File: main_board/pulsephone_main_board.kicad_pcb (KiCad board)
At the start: 4 copper layers, 70.5 x 128.5 mm, 51 parts, among them J1 USB_C_Receptacle_USB2.0_14P, J2 Conn_01x05, J3 Conn_2Rows-35Pins_MountingPin, J4 Conn_2Rows-35Pins_MountingPin, J5 Conn_2Rows-35Pins_MountingPin, J7 Micro_SD_Card_Det1, SW1 SW_Push, SW2 SW_Push, U1 XL1509-3.3, U2 PCM5102APWR, U5 TP4056-42-ESOP8

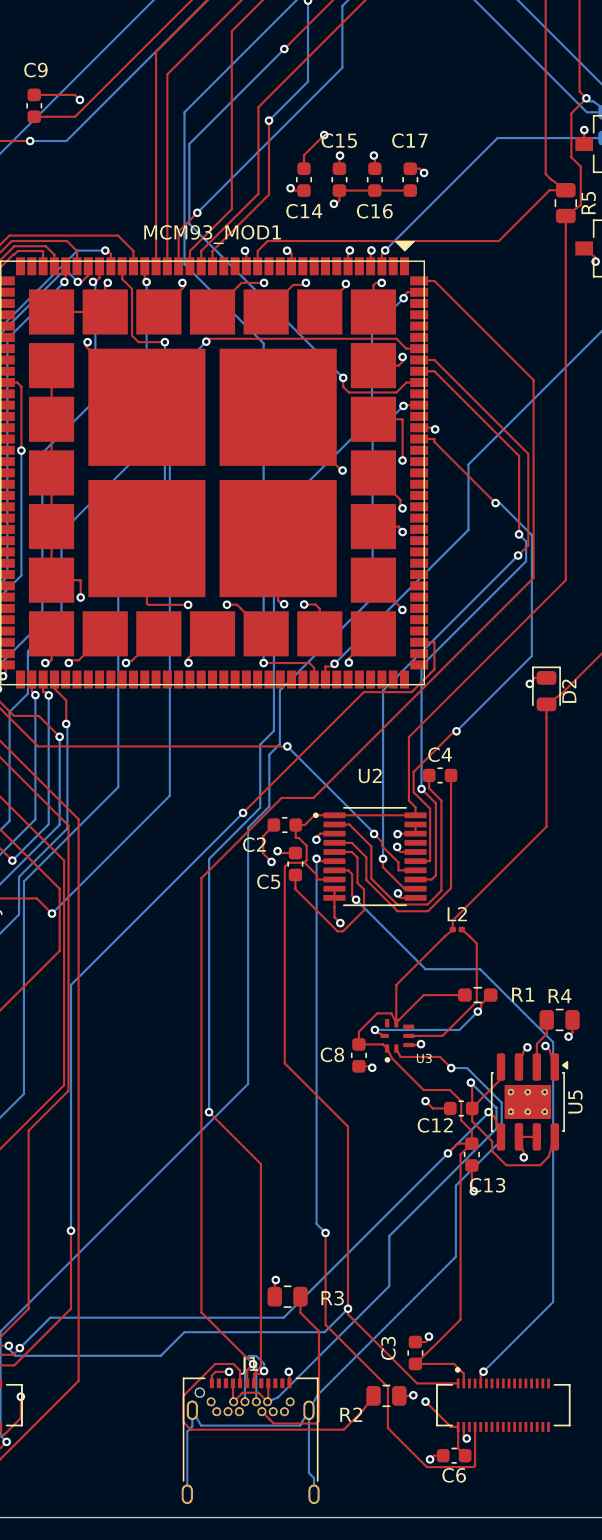
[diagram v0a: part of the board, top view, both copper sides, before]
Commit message: more smoothing caps, and making sure board is compliant with CompuLab Standards
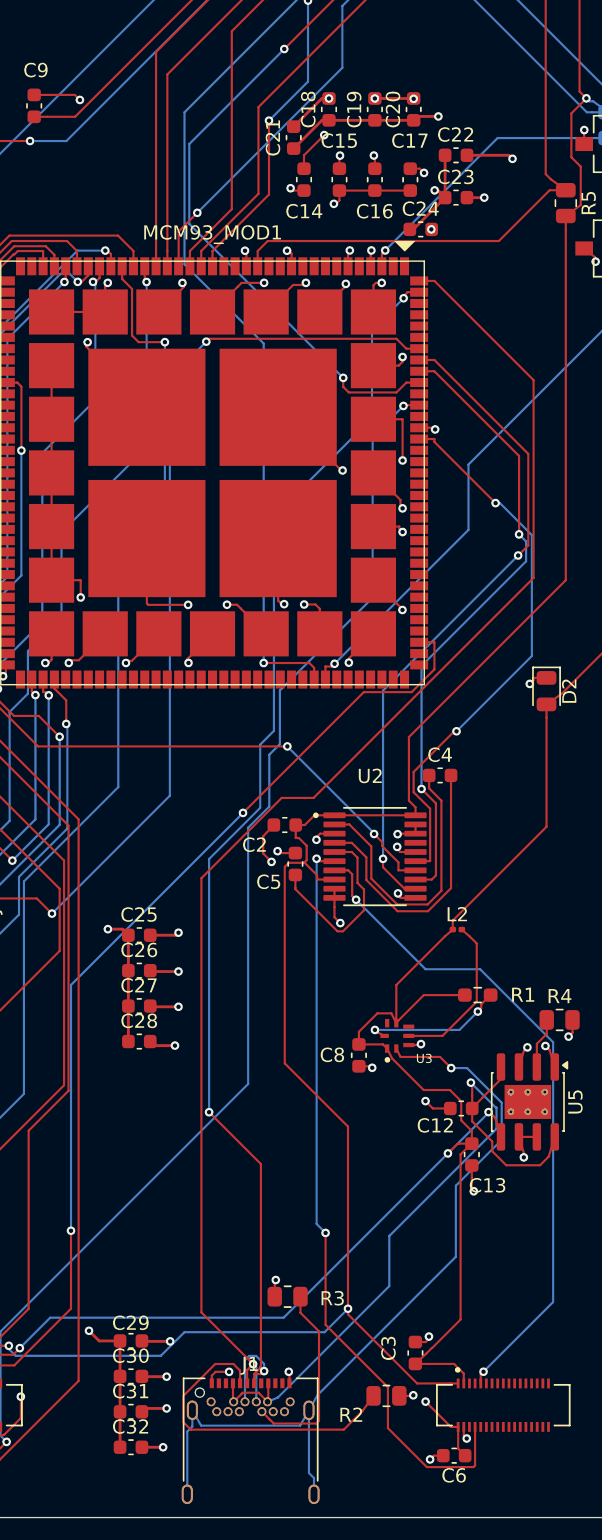
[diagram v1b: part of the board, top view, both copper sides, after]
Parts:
- added C18: 22uF, Capacitor_SMD:C_0603_1608Metric, F.Cu at (143.2, 54.8)
- added C19: 22uF, Capacitor_SMD:C_0603_1608Metric, F.Cu at (146.5, 54.8)
- added C20: 22uF, Capacitor_SMD:C_0603_1608Metric, F.Cu at (149.2, 54.8)
- added C21: 22uF, Capacitor_SMD:C_0603_1608Metric, F.Cu at (140.8, 56.8)
- added C22: 22uF, Capacitor_SMD:C_0603_1608Metric, F.Cu at (152.2, 58.0)
- added C23: 22uF, Capacitor_SMD:C_0603_1608Metric, F.Cu at (152.2, 61.0)
- added C24: 22uF, Capacitor_SMD:C_0603_1608Metric, F.Cu at (149.8, 63.2)
- added C25: 22uF, Capacitor_SMD:C_0603_1608Metric, F.Cu at (129.8, 113.2)
- added C26: 22uF, Capacitor_SMD:C_0603_1608Metric, F.Cu at (129.8, 115.8)
- added C27: 22uF, Capacitor_SMD:C_0603_1608Metric, F.Cu at (129.8, 118.3)
- added C28: 22uF, Capacitor_SMD:C_0603_1608Metric, F.Cu at (129.8, 120.8)
- added C29: 22uF, Capacitor_SMD:C_0603_1608Metric, F.Cu at (129.2, 142.0)
- added C30: 22uF, Capacitor_SMD:C_0603_1608Metric, F.Cu at (129.2, 144.5)
- added C31: 22uF, Capacitor_SMD:C_0603_1608Metric, F.Cu at (129.2, 147.0)
- added C32: 22uF, Capacitor_SMD:C_0603_1608Metric, F.Cu at (129.2, 149.5)
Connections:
- MCM93_MOD1 pad 76: unconnected-(MCM93_MOD1C-6-Pad76) -> SD2_CD_B
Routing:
- net +5V: track 32.2 -> 70.0 mm, vias 12 -> 16
- net GND: track 213.5 -> 239.2 mm, vias 81 -> 95

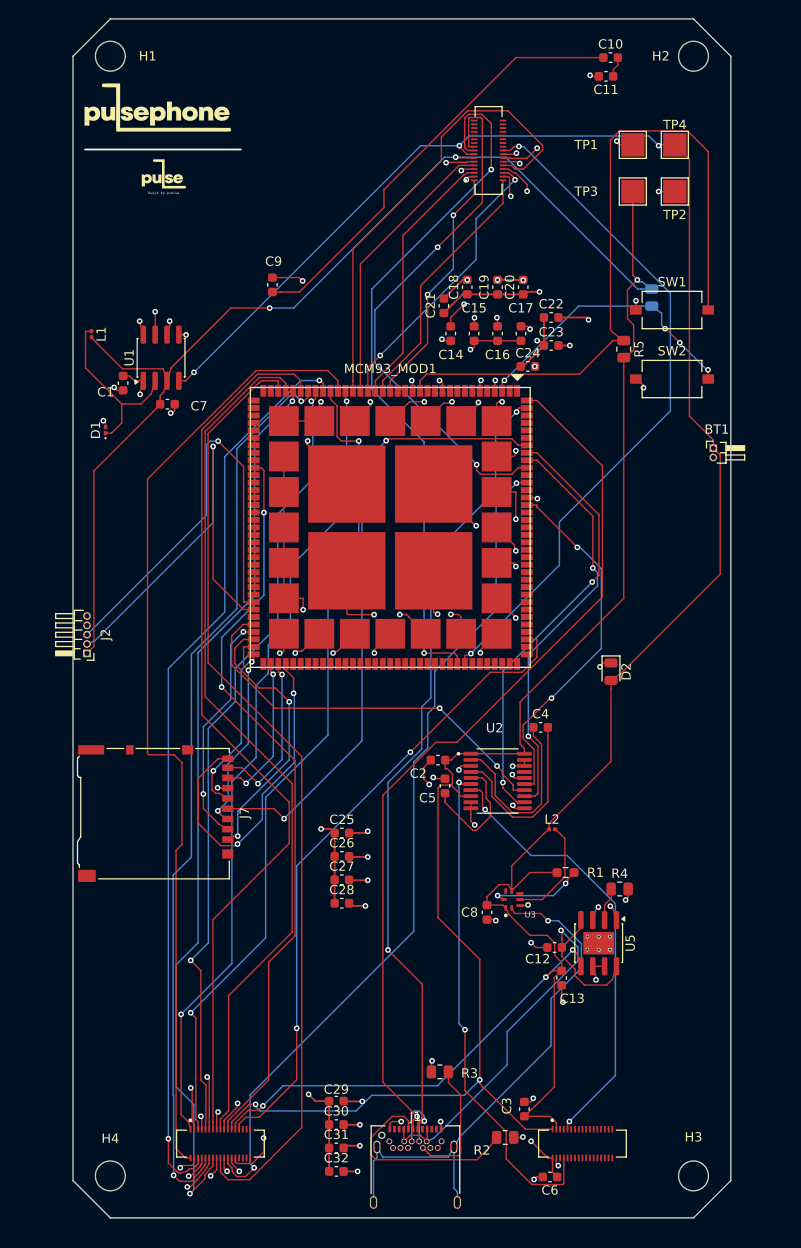
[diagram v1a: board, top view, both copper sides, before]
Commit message: fix PCB design errors, and fix power LED circuitry.
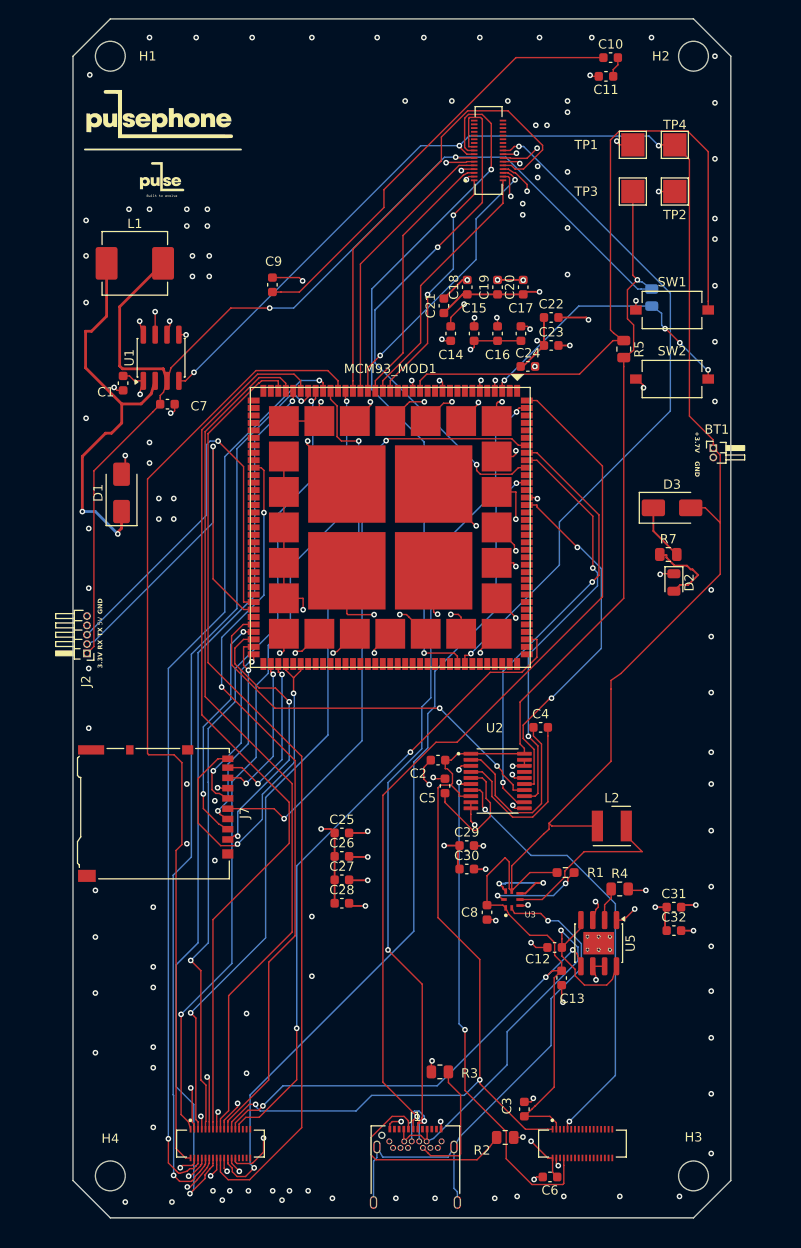
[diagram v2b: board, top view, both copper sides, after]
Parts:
- added D3: D_Schottky, Diode_SMD:D_SMA, F.Cu at (165.2, 78.4)
- added R7: 1kΩ, Resistor_SMD:R_0805_2012Metric, F.Cu at (164.8, 83.4)
- C1, C7: value 20uF -> 22uF
- D1: footprint Diode_SMD:D_0201_0603Metric -> Diode_SMD:D_SMA
- L1: footprint Inductor_SMD:L_0201_0603Metric -> Inductor_SMD:L_APV_APH0650
- L2: footprint Inductor_SMD:L_0201_0603Metric -> Inductor_SMD_Wurth:L_Wurth_WE-LQSH-4020
- moved C32 44.4 mm to (165.4, 123.7)
- moved C31 44.4 mm to (165.4, 121.2)
- moved C29 30.7 mm to (143.2, 114.6)
- moved C30 30.7 mm to (143.2, 117.1)
- moved D2 11.7 mm to (165.4, 86.4)
- moved L1 8.90 mm to (107.6, 52.2), turned to 0 degrees
- moved D1 6.93 mm to (106.2, 76.8)
- moved L2 6.42 mm to (158.8, 112.5)
- moved G*** 0.73 mm to (110.2, 36.2)
- moved G*** 0.36 mm to (110.5, 43.3)
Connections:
- D2 pad 2: +3.7VBAT -> Net-(D2-A)
- U3 pad 5: (no net) -> +5V
- U3 pad 7: (no net) -> +5V
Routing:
- net Net-(D1-K): track 19.3 -> 44.1 mm, vias 0 -> 2
- net +3.7VBAT: track 250.8 -> 265.1 mm
- net +3.3V: track 271.3 -> 279.9 mm
- net Net-(D2-A): track 0.00 -> 8.49 mm
- net Net-(U3-SW): track 11.4 -> 19.1 mm
- net +5V: track 70.0 -> 76.3 mm, vias 16 -> 19
- net Net-(D3-K): track 0.00 -> 6.04 mm
- net GND: track 239.2 -> 241.6 mm, vias 95 -> 200
- net SD2_CD_B: track 36.3 -> 38.1 mm
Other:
- board text added: "+3.7V"
- board text added: "3.3V"
- board text added: "5V"
- board text added: "GND"
- board text added: "RX"
- board text added: "TX"

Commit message: git stuff
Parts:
- L1: footprint Inductor_SMD:L_APV_APH0650 -> Inductor_SMD:L_APV_APH0630
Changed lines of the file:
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@@
 		)
 	)
-	(footprint "Inductor_SMD:L_APV_APH0650"
+	(footprint "Inductor_SMD:L_APV_APH0630"
 		(layer "F.Cu")
 		(at 107.625 52.2)
-		(descr "Inductor, APV, APH0650, 6.8x6.6x4.8mm, (http://en.apvind.com/public/upload/20240408/996aafa961154ed753e4983e7eb80fa7.pdf), generated with kicad-footprint-generator gen_inductor.py")
+		(descr "Inductor, APV, APH0630, 6.8x6.6x2.8mm, (http://en.apvind.com/public/upload/20240408/996aafa961154ed753e4983e7eb80fa7.pdf), generated with kicad-footprint-generator gen_inductor.py")
 		(tags "molded power shielded")
 		(property "Reference" "L1"
@@
 			)
 		)
-		(property "Datasheet" "~"
+		(property "Datasheet" ""
 			(at 0 0 0)
 			(layer "F.Fab")
@@
 			)
 		)
-		(property "Description" "Inductor"
+		(property "Description" ""
 			(at 0 0 0)
 			(layer "F.Fab")
@@
 		)
 		(embedded_fonts no)
-		(model "${KICAD9_3DMODEL_DIR}/Inductor_SMD.3dshapes/L_APV_APH0650.step"
+		(model "${KICAD9_3DMODEL_DIR}/Inductor_SMD.3dshapes/L_APV_APH0630.step"
 			(offset
 				(xyz 0 0 0)

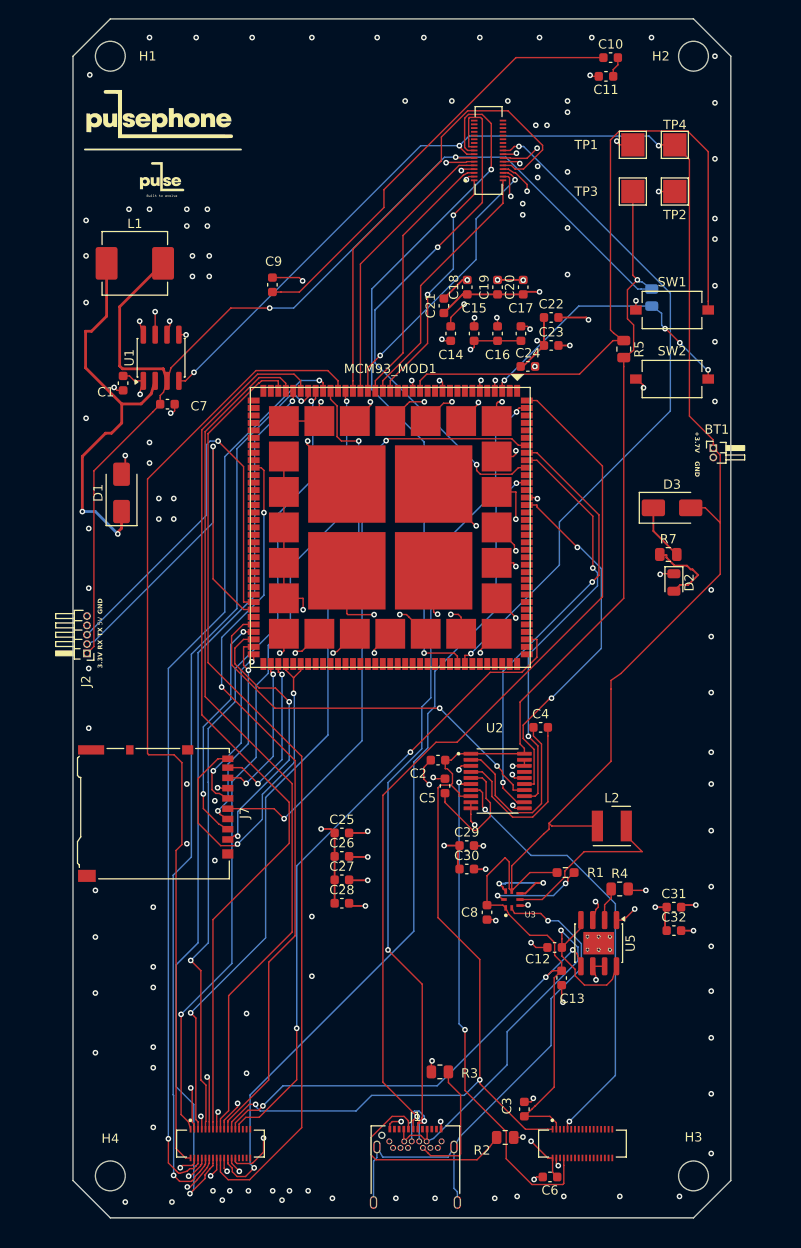
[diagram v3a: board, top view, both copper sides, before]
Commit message: add 3.7v regulator to VBAT for a stable vbat voltage.
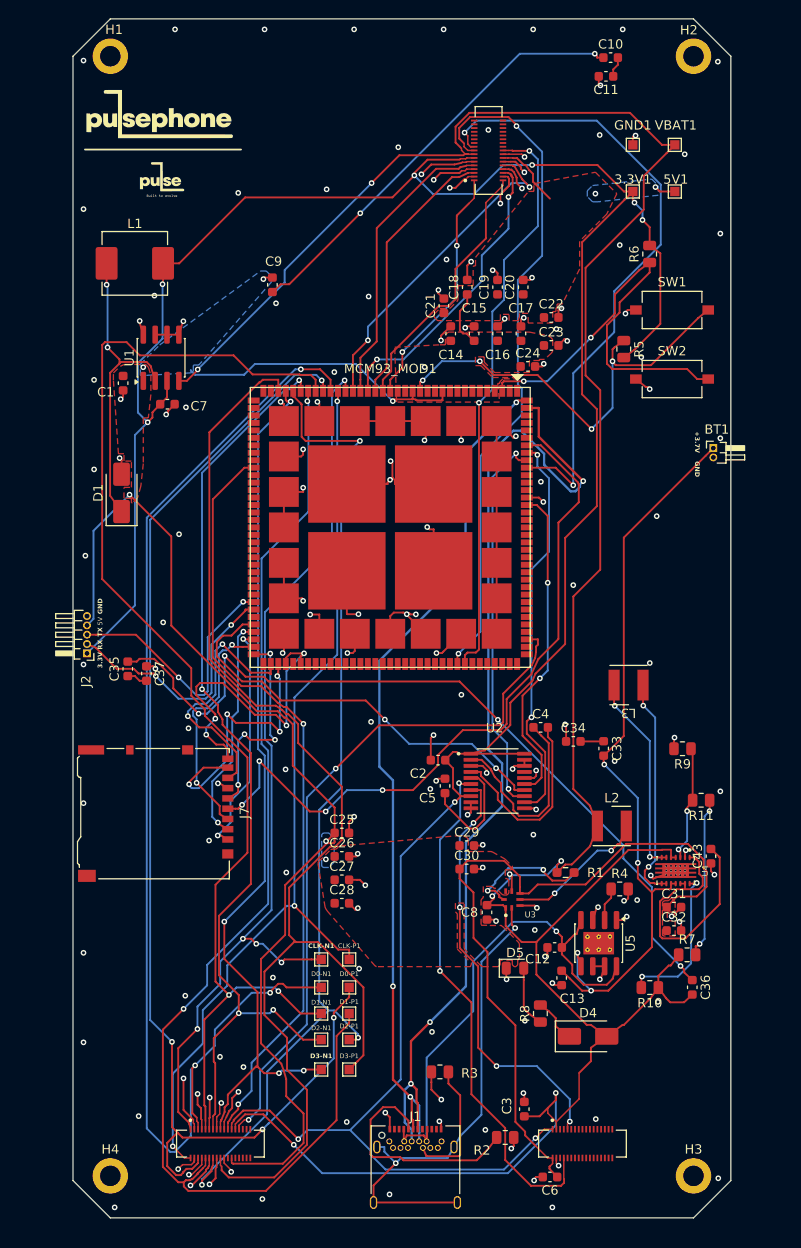
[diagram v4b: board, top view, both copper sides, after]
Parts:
- removed D2: LED, LED_SMD:LED_0805_2012Metric
- removed D3: D_Schottky, Diode_SMD:D_SMA
- added C33: 10uF, Capacitor_SMD:C_0603_1608Metric, F.Cu at (157.9, 104.2)
- added C34: 10uF, Capacitor_SMD:C_0603_1608Metric, F.Cu at (154.6, 103.4)
- added C35: 22uF, Capacitor_SMD:C_0603_1608Metric, F.Cu at (106.9, 95.7)
- added C36: 22uF, Capacitor_SMD:C_0603_1608Metric, F.Cu at (167.4, 129.8)
- added C37: 22uF, Capacitor_SMD:C_0603_1608Metric, F.Cu at (108.9, 96.2)
- added C43: 100nF, Capacitor_SMD:C_0603_1608Metric, F.Cu at (169.4, 115.7)
- added CLK-N1: TestPoint, TestPoint:TestPoint_Pad_1.0x1.0mm, F.Cu at (127.6, 126.8)
- added CLK-P1: TestPoint, TestPoint:TestPoint_Pad_1.0x1.0mm, F.Cu at (130.6, 126.8)
- added D0-N1: TestPoint, TestPoint:TestPoint_Pad_1.0x1.0mm, F.Cu at (127.6, 129.8)
- added D0-P1: TestPoint, TestPoint:TestPoint_Pad_1.0x1.0mm, F.Cu at (130.6, 129.8)
- added D1-N1: TestPoint, TestPoint:TestPoint_Pad_1.0x1.0mm, F.Cu at (127.6, 132.6)
- added D1-P1: TestPoint, TestPoint:TestPoint_Pad_1.0x1.0mm, F.Cu at (130.6, 132.6)
- added D2-N1: TestPoint, TestPoint:TestPoint_Pad_1.0x1.0mm, F.Cu at (127.6, 135.4)
- added D2-P1: TestPoint, TestPoint:TestPoint_Pad_1.0x1.0mm, F.Cu at (130.6, 135.4)
- added D3-N1: TestPoint, TestPoint:TestPoint_Pad_1.0x1.0mm, F.Cu at (127.6, 138.6)
- added D3-P1: TestPoint, TestPoint:TestPoint_Pad_1.0x1.0mm, F.Cu at (130.6, 138.6)
- added D4: D_Schottky, Diode_SMD:D_SMA, F.Cu at (156.2, 135.0)
- added D5: LED, LED_SMD:LED_0805_2012Metric, F.Cu at (148.4, 127.7)
- added L3: 1.5uH, Inductor_SMD_Wurth:L_Wurth_WE-LQSH-4020, F.Cu at (160.5, 97.4)
- added R10: 1 MΩ, Resistor_SMD:R_0805_2012Metric, F.Cu at (162.8, 129.8)
- added R11: 51 kΩ, Resistor_SMD:R_0805_2012Metric, F.Cu at (168.3, 109.7)
- added R8: 1kΩ, Resistor_SMD:R_0805_2012Metric, F.Cu at (151.1, 132.6)
- added R9: 180 kΩ, Resistor_SMD:R_0805_2012Metric, F.Cu at (166.3, 104.2)
- added U4: TPS63020DSJR/3.7V Reg, TPS63020:IC_TPS63020DSJR, F.Cu at (165.6, 117.3)
- 3.3V1: renamed from TP3; footprint TestPoint:TestPoint_Pad_2.5x2.5mm -> TestPoint:TestPoint_Pad_1.0x1.0mm
- 5V1: renamed from TP2; footprint TestPoint:TestPoint_Pad_2.5x2.5mm -> TestPoint:TestPoint_Pad_1.0x1.0mm
- GND1: renamed from TP1; footprint TestPoint:TestPoint_Pad_2.5x2.5mm -> TestPoint:TestPoint_Pad_1.0x1.0mm
- H1, H2, H3, H4: footprint MountingHole:MountingHole_3.2mm_M3 -> MountingHole:MountingHole_2.2mm_M2_DIN965_Pad
- R6: moved to F.Cu
- R7: value 1kΩ -> 1.1 MΩ
- VBAT1: renamed from TP4; footprint TestPoint:TestPoint_Pad_2.5x2.5mm -> TestPoint:TestPoint_Pad_1.0x1.0mm
- moved R7 43.0 mm to (166.8, 126.3)
- moved R6 4.67 mm to (162.8, 51.2)
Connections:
- BT1 pad 1: +3.7VBAT -> Net-(BT1-+)
- C13 pad 2: +3.7VBAT -> Net-(BT1-+)
- R7 pad 1: Net-(D2-A) -> +3.7VBAT
- U5 pad 5: +3.7VBAT -> Net-(BT1-+)
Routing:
- net +5V: track 76.3 -> 238.2 mm, vias 19 -> 8
- net /I2C3_SDA: track 91.1 -> 0.00 mm, vias 2 -> 0
- net Net-(C35-Pad2): track 0.00 -> 87.3 mm, vias 0 -> 4
- net Net-(BT1-+): track 0.00 -> 82.4 mm, vias 0 -> 4
- net /DSI_D1_N: track 85.6 -> 131.0 mm
- net /DSI_D0_N: track 89.3 -> 133.2 mm, vias 2 -> 3
- net /DSI_D0_P: track 97.7 -> 130.8 mm, vias 2 -> 4
- net /DSI_D1_P: track 97.1 -> 129.3 mm
- net /DSI_D3_P: track 102.4 -> 131.9 mm
- net RESET: track 75.7 -> 47.1 mm, vias 0 -> 4
- net +3.7VBAT: track 265.1 -> 293.6 mm, vias 6 -> 7
- net Net-(U4-EN): track 0.00 -> 28.4 mm
- net L_1: track 0.00 -> 24.2 mm, vias 0 -> 2
- net +3.3V: track 279.9 -> 302.8 mm, vias 5 -> 9
- net L_2: track 0.00 -> 21.8 mm, vias 0 -> 2
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- added copper zone on B.Cu, net +5V
- added copper zone on F.Cu, net +5V
- added copper zone on In2.Cu, net GND
- removed copper zone on In2.Cu, net +5V

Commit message: fixes
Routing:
- net /I2C3_SDA: track 0.00 -> 102.0 mm, vias 0 -> 3
- net /DSI_D3_N: track 93.6 -> 136.6 mm
- net /DSI_D2_N: track 102.1 -> 106.0 mm
- net /DSI_CLK_N: track 99.5 -> 100.7 mm
- net /DSI_D3_P: track 131.9 -> 133.1 mm
